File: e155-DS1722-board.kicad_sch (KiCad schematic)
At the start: 13 parts, among them J1 Conn_01x08, J2 Conn_01x08

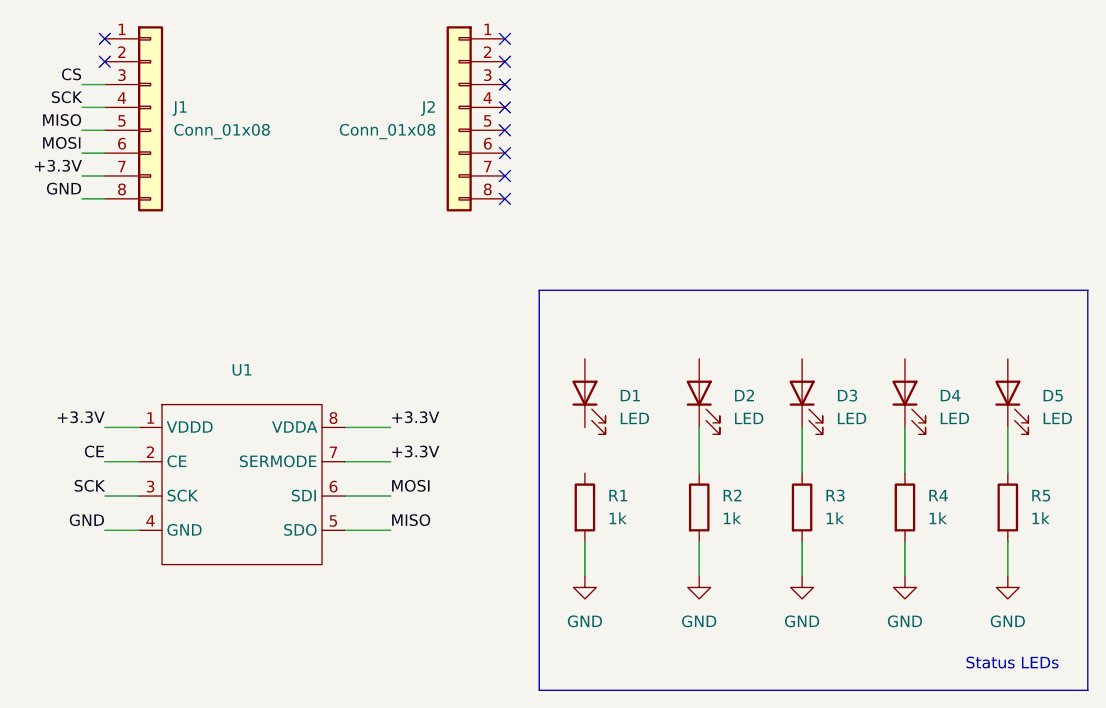
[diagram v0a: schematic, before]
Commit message: Initial PCB layout and routing
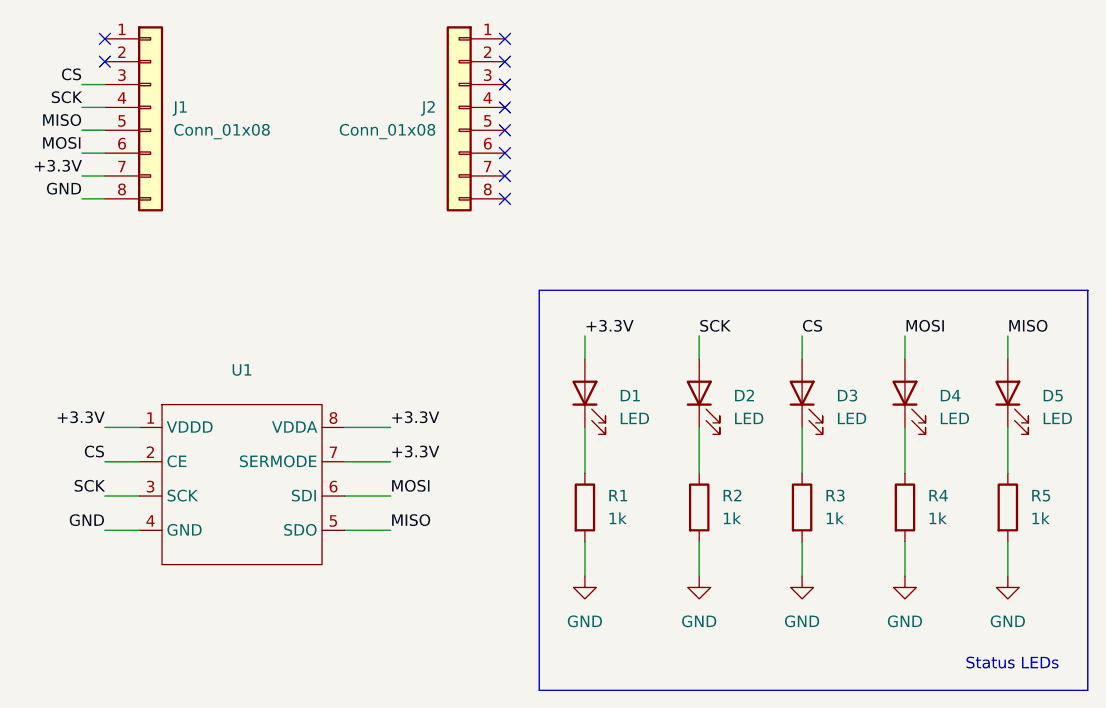
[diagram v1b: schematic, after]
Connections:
- net CE is gone; now on net CS: U1.2 (CE)
- net +3.3V: now also D1.2 (A)
- net CS: now also D3.2 (A)
- net MISO: now also D5.2 (A)
- net MOSI: now also D4.2 (A)
- net SCK: now also D2.2 (A)
- net at D1.1 (K): now also R1.1
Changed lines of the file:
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@@
+	(wire
+		(pts
+			(xy 222.25 121.92) (xy 222.25 124.46)
+		)
+		(stroke
+			(width 0)
+			(type default)
+		)
+	)
+	(wire
+		(pts
+			(xy 222.25 132.08) (xy 222.25 137.16)
+		)
+		(stroke
+			(width 0)
+			(type default)
+		)
+	)
 	(wire
 		(pts
@@
 	(wire
 		(pts
+			(xy 269.24 121.92) (xy 269.24 124.46)
+		)
+		(stroke
+			(width 0)
+			(type default)
+		)
+	)
+	(wire
+		(pts
 			(xy 166.37 104.14) (xy 168.91 104.14)
 		)
@@
 	(wire
 		(pts
+			(xy 257.81 121.92) (xy 257.81 124.46)
+		)
+		(stroke
+			(width 0)
+			(type default)
+		)
+	)
+	(wire
+		(pts
 			(xy 222.25 144.78) (xy 222.25 148.59)
 		)
@@
 		(pts
 			(xy 168.91 135.89) (xy 172.72 135.89)
+		)
+		(stroke
+			(width 0)
+			(type default)
+		)
+	)
+	(wire
+		(pts
+			(xy 246.38 121.92) (xy 246.38 124.46)
+		)
+		(stroke
+			(width 0)
+			(type default)
+		)
+	)
+	(wire
+		(pts
+			(xy 234.95 121.92) (xy 234.95 124.46)
 		)
 		(stroke
@@
 		)
 	)
-	(label "CE"
+	(label "MOSI"
+		(at 257.81 121.92 0)
+		(fields_autoplaced yes)
+		(effects
+			(font
+				(size 1.27 1.27)
+			)
+			(justify left bottom)
+		)
+	)
+	(label "CS"
 		(at 168.91 135.89 180)
 		(fields_autoplaced yes)
@@
 		)
 	)
+	(label "CS"
+		(at 246.38 121.92 0)
+		(fields_autoplaced yes)
+		(effects
+			(font
+				(size 1.27 1.27)
+			)
+			(justify left bottom)
+		)
+	)
 	(label "+3.3V"
 		(at 166.37 104.14 180)
@@
 		)
 	)
+	(label "+3.3V"
+		(at 222.25 121.92 0)
+		(fields_autoplaced yes)
+		(effects
+			(font
+				(size 1.27 1.27)
+			)
+			(justify left bottom)
+		)
+	)
 	(label "MOSI"
 		(at 166.37 101.6 180)
@@
 		)
 	)
+	(label "SCK"
+		(at 234.95 121.92 0)
+		(fields_autoplaced yes)
+		(effects
+			(font
+				(size 1.27 1.27)
+			)
+			(justify left bottom)
+		)
+	)
+	(label "MISO"
+		(at 269.24 121.92 0)
+		(fields_autoplaced yes)
+		(effects
+			(font
+				(size 1.27 1.27)
+			)
+			(justify left bottom)
+		)
+	)
